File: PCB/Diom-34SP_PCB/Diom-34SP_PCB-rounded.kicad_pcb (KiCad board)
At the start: 2 copper layers, 133.5 x 101.1 mm, 30 parts, among them J1 Conn_01x02_Male, SW1 SHOU_HAN_MSK12C02-HB, U1 nice_nano

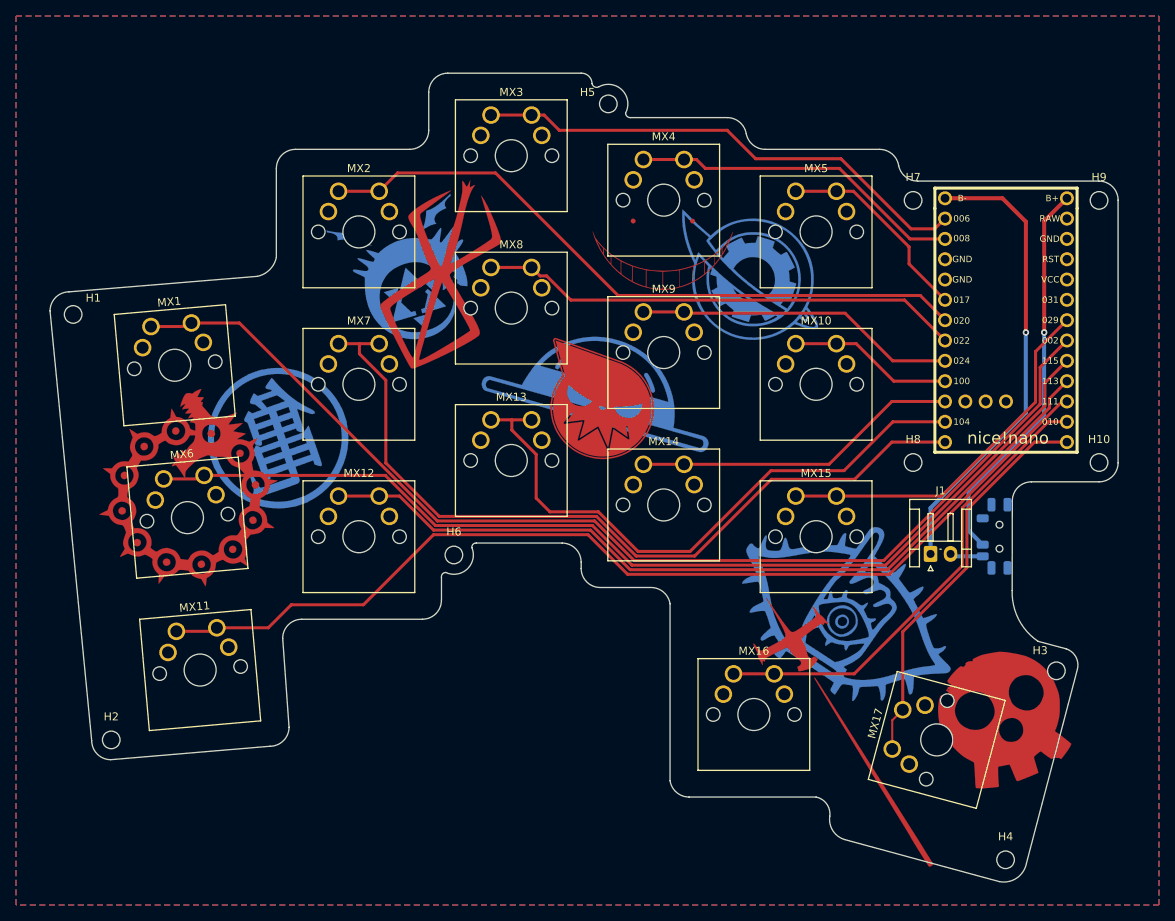
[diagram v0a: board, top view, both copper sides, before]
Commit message: Moved Artwork, Tracks, Rounded PCB
Also Gerbers
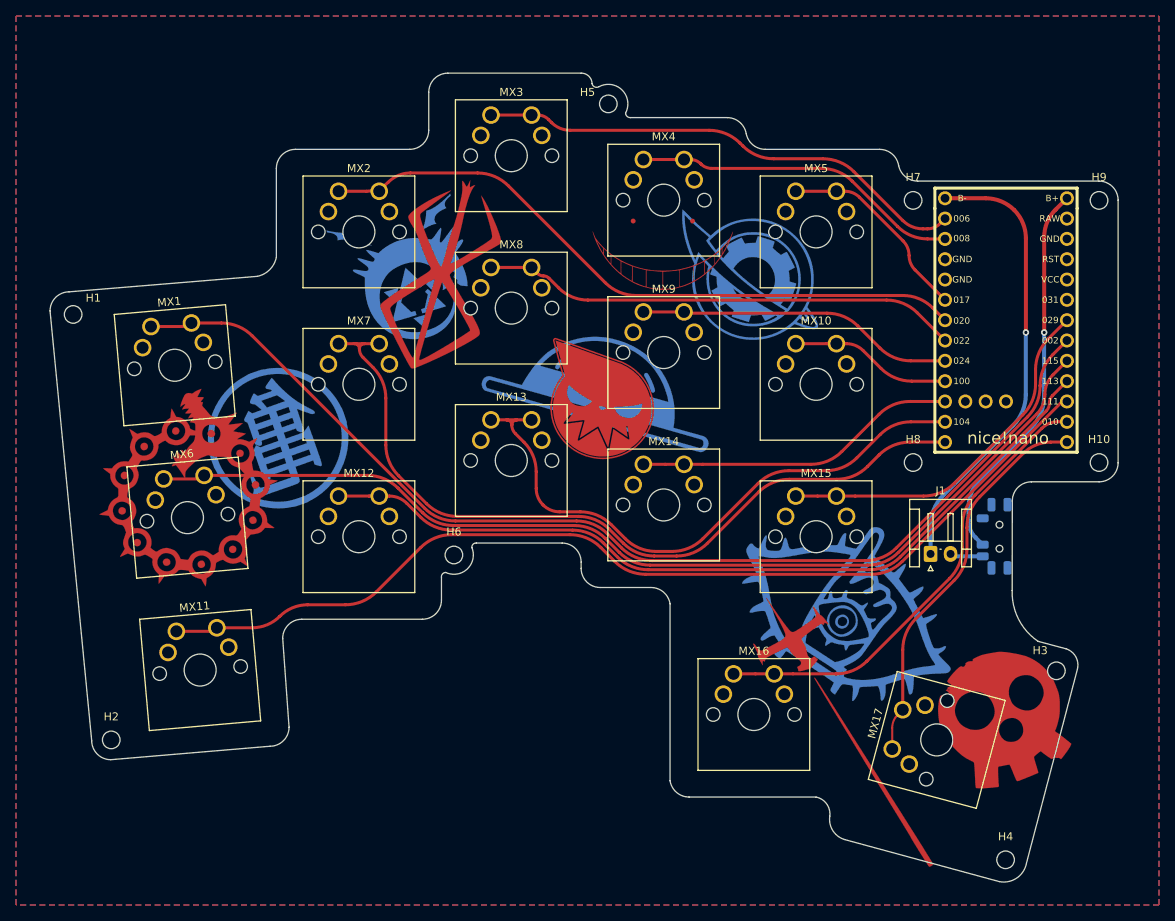
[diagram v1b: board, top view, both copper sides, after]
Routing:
- net MX1: track 141.1 -> 139.2 mm
- net MX11: track 127.3 -> 125.4 mm
- net MX6: track 130.0 -> 128.3 mm
- net MX12: track 105.3 -> 104.0 mm
- net MX3: track 63.2 -> 61.9 mm
- net MX17: track 49.8 -> 48.5 mm
- net MX2: track 84.4 -> 83.2 mm
- net MX7: track 102.0 -> 100.9 mm
- net B-: track 57.8 -> 56.8 mm
- net MX16: track 59.0 -> 58.0 mm
- net B+: track 49.1 -> 48.2 mm
- net MX13: track 76.7 -> 75.8 mm
- net MX15: track 46.7 -> 45.9 mm
- net MX4: track 41.8 -> 41.1 mm
- net MX8: track 60.5 -> 59.8 mm
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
